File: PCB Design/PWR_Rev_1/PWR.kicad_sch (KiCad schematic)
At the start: 57 parts, among them J1 Conn_01x24_Pin, J2 Conn_01x24_Pin, U1 LMR33630ADDA, U2 LMR33630ADDA, U3 LMR33630ADDA

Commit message: Cleaned up Formating
Cleaned up formatting and added required exports for delivery
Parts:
- R7: value 100k -> N/A
- R9: value 9.09k -> N/A
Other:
- note added: "BOARD CONNECTORS"
- company: (none) -> CAPSTONE
- title: (none) -> SWARM PWR BOARD
- moved on the sheet: C28, C29, D1, D2, D3, D4, D5, F1, H1, H2, J1, J2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

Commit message: Small Updates
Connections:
- net GND: now also D5.2 (A); no longer D5.1 (K)
- net at D4.2 (A), F1.2: now also D5.1 (K); no longer D5.2 (A)
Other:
- moved on the sheet: D5
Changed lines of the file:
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@@
 	(symbol
 		(lib_id "Diode:PTVS5V0Z1USK")
-		(at 148.59 105.41 90)
+		(at 148.59 105.41 270)
 		(unit 1)
 		(exclude_from_sim no)
@@
 		(dnp no)
 		(property "Reference" "D5"
-			(at 149.86 105.41 90)
+			(at 147.32 105.41 90)
 			(effects
 				(font
@@
 		)
 		(property "Value" "SMBJ18A"
-			(at 148.844 107.95 90)
+			(at 148.082 107.95 90)
 			(effects
 				(font
@@
 		)
 		(property "Footprint" "Diode_SMD:D_SMB"
-			(at 153.035 105.41 0)
+			(at 144.145 105.41 0)
 			(effects
 				(font

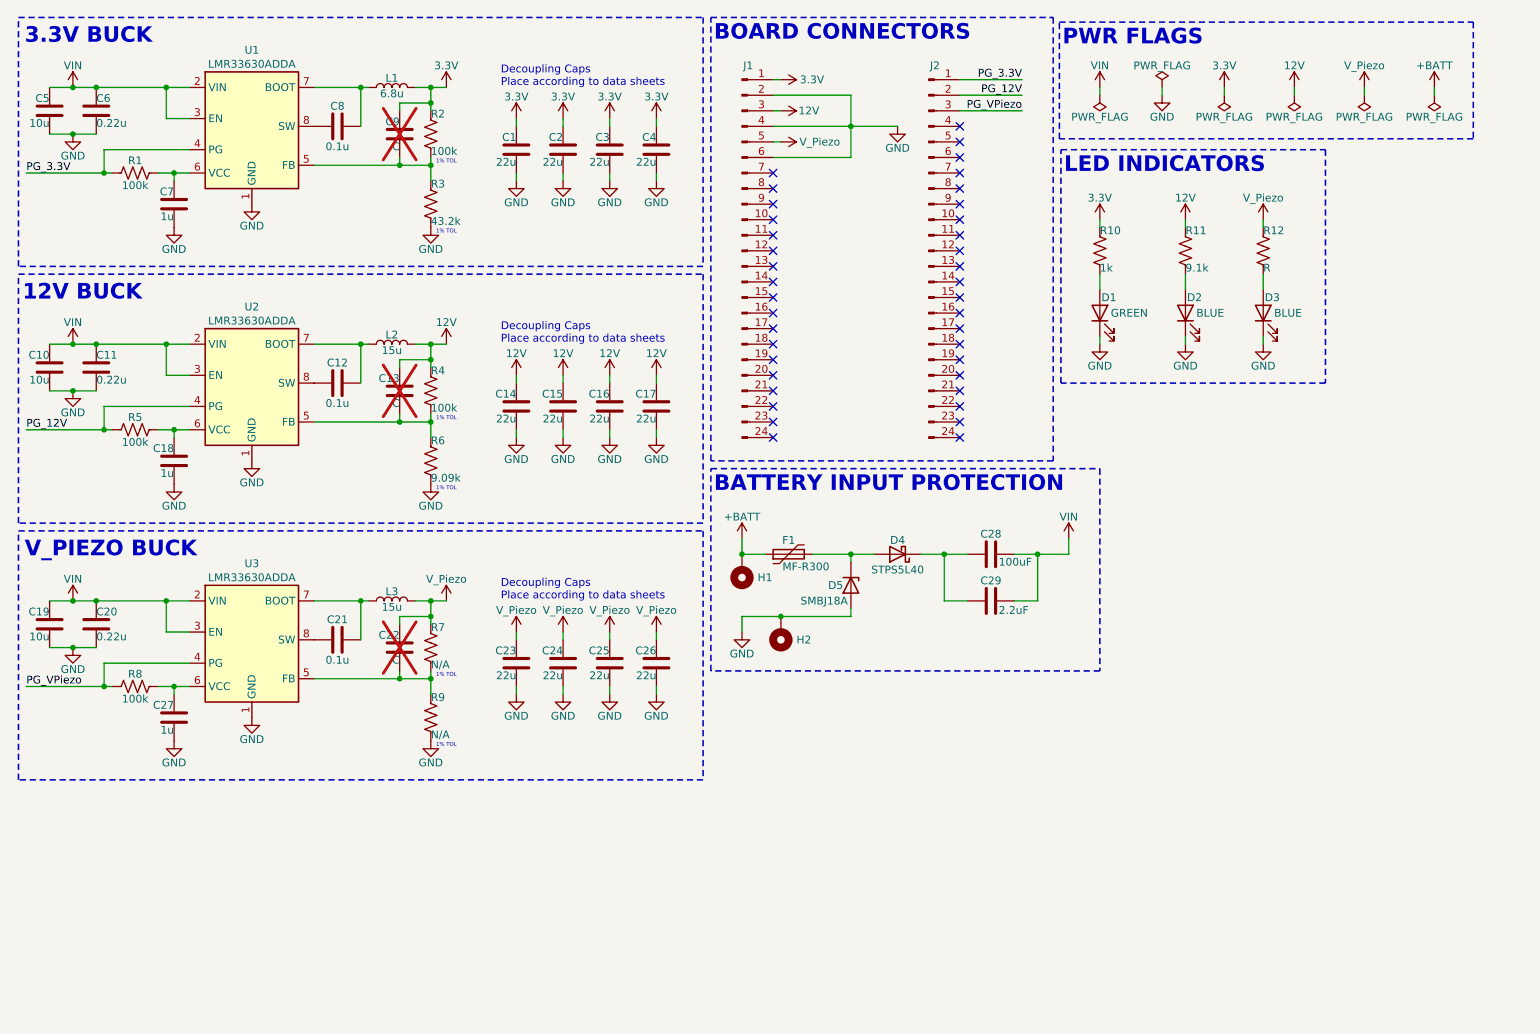
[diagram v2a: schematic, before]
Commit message: Fixed Schematic Errors
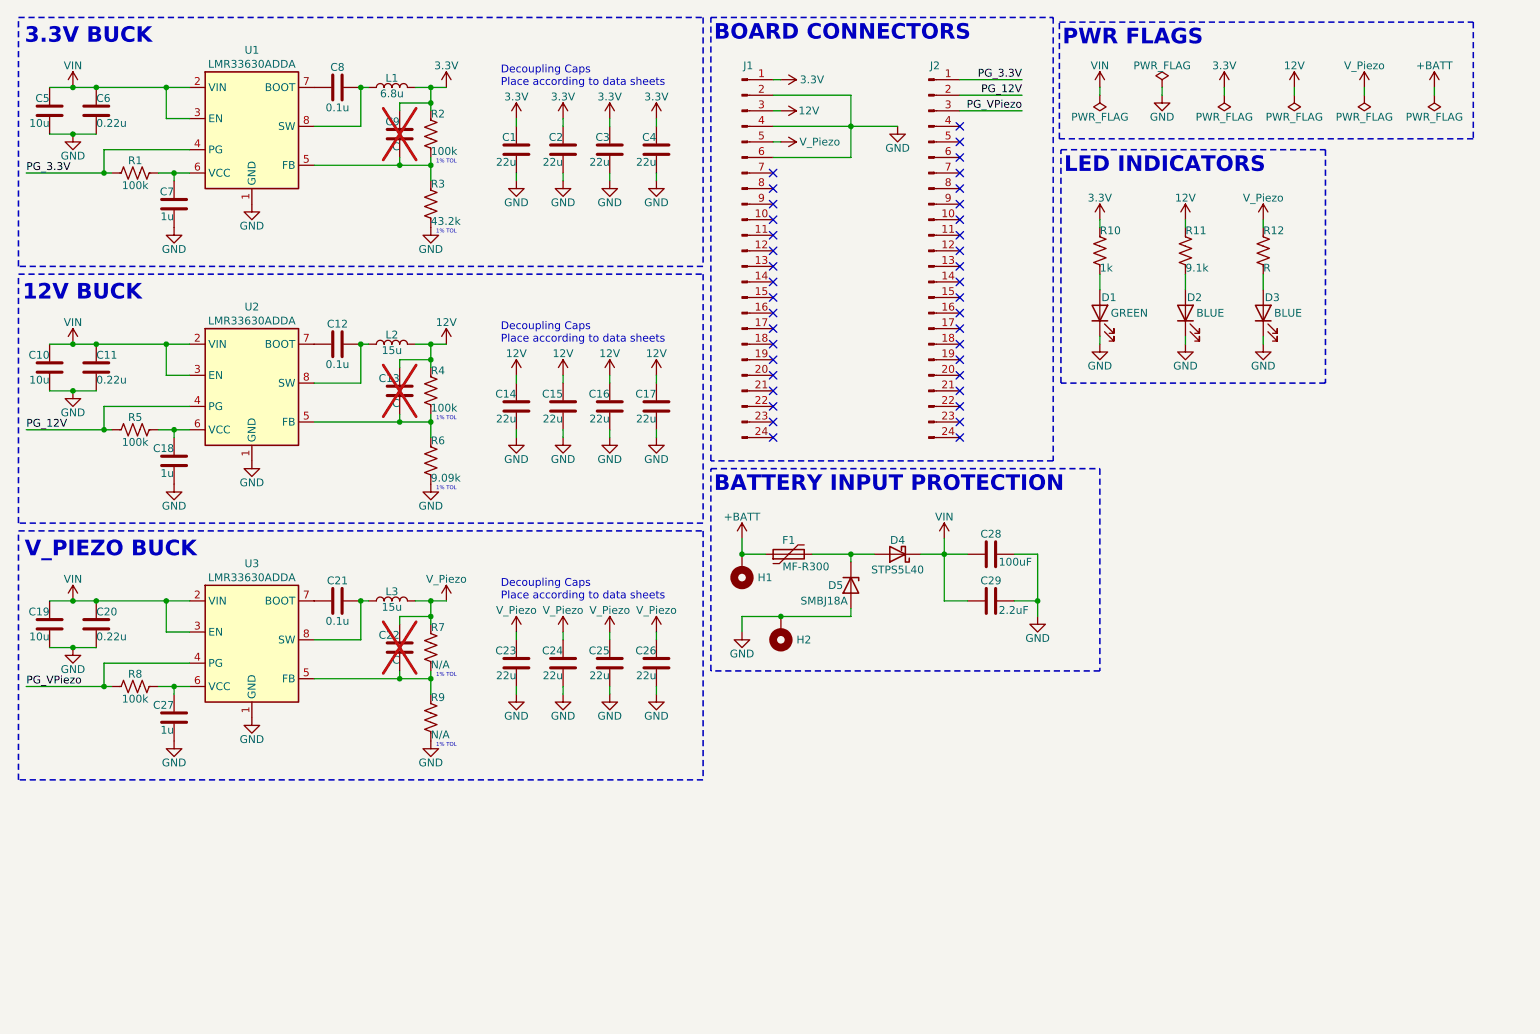
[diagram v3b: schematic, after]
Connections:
- net GND: now also C28.2, C29.2
- net VIN: now also C28.1, C29.1, D4.1 (K); no longer C28.2, C29.2
- net at C12.1, L2.1: now also U2.8 (SW); no longer U2.7 (BOOT)
- net at C12.2: now also U2.7 (BOOT); no longer U2.8 (SW)
- net at C8.1, L1.1: now also U1.8 (SW); no longer U1.7 (BOOT)
- net at C8.2: now also U1.7 (BOOT); no longer U1.8 (SW)
- net at C21.1, L3.1: now also U3.8 (SW); no longer U3.7 (BOOT)
- net at C21.2: now also U3.7 (BOOT); no longer U3.8 (SW)
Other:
- moved on the sheet: C12, C21, C8

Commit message: Added PWR Export Files
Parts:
- L3: value 15u -> N/A
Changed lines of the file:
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@@
 	(title_block
 		(title "SWARM PWR BOARD")
-		(date "2026-03-21")
+		(date "2026-03-23")
 		(rev "1.1")
 		(company "CAPSTONE")
@@
 			)
 		)
-		(property "Value" "15u"
+		(property "Value" "N/A"
 			(at 73.66 108.966 90)
 			(effects

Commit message: PWR - Updated 3D Models for Full Board Export
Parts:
- F1: footprint Fuse:Fuse_Bourns_MF-RHT300 -> PWR_Library:Fuse_Bourns_MF-RHT300
- L1, L2, L3: footprint Inductor_SMD:L_Wuerth_MAPI-5030 -> PWR_Library:L_Wuerth_MAPI-5030
- U1, U2, U3: footprint Package_SO:Texas_HSOP-8-1EP_3.9x4.9mm_P1.27mm_ThermalVias -> PWR_Library:Texas_HSOP-8-1EP_3.9x4.9mm_P1.27mm_ThermalVias
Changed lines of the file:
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@@
 			)
 		)
-		(property "Footprint" "Package_SO:Texas_HSOP-8-1EP_3.9x4.9mm_P1.27mm_ThermalVias"
+		(property "Footprint" "PWR_Library:Texas_HSOP-8-1EP_3.9x4.9mm_P1.27mm_ThermalVias"
 			(at 50.8 91.44 0)
 			(effects
@@
 			)
 		)
-		(property "Footprint" "Inductor_SMD:L_Wuerth_MAPI-5030"
+		(property "Footprint" "PWR_Library:L_Wuerth_MAPI-5030"
 			(at 73.66 66.04 0)
 			(effects
@@
 			)
 		)
-		(property "Footprint" "Fuse:Fuse_Bourns_MF-RHT300"
+		(property "Footprint" "PWR_Library:Fuse_Bourns_MF-RHT300"
 			(at 143.51 99.06 0)
 			(effects
@@
 			)
 		)
-		(property "Footprint" "Package_SO:Texas_HSOP-8-1EP_3.9x4.9mm_P1.27mm_ThermalVias"
+		(property "Footprint" "PWR_Library:Texas_HSOP-8-1EP_3.9x4.9mm_P1.27mm_ThermalVias"
 			(at 50.8 49.53 0)
 			(effects
@@
 			)
 		)
-		(property "Footprint" "Inductor_SMD:L_Wuerth_MAPI-5030"
+		(property "Footprint" "PWR_Library:L_Wuerth_MAPI-5030"
 			(at 73.66 24.13 0)
 			(effects
@@
 			)
 		)
-		(property "Footprint" "Inductor_SMD:L_Wuerth_MAPI-5030"
+		(property "Footprint" "PWR_Library:L_Wuerth_MAPI-5030"
 			(at 73.66 107.95 0)
 			(effects
@@
 			)
 		)
-		(property "Footprint" "Package_SO:Texas_HSOP-8-1EP_3.9x4.9mm_P1.27mm_ThermalVias"
+		(property "Footprint" "PWR_Library:Texas_HSOP-8-1EP_3.9x4.9mm_P1.27mm_ThermalVias"
 			(at 50.8 133.35 0)
 			(effects

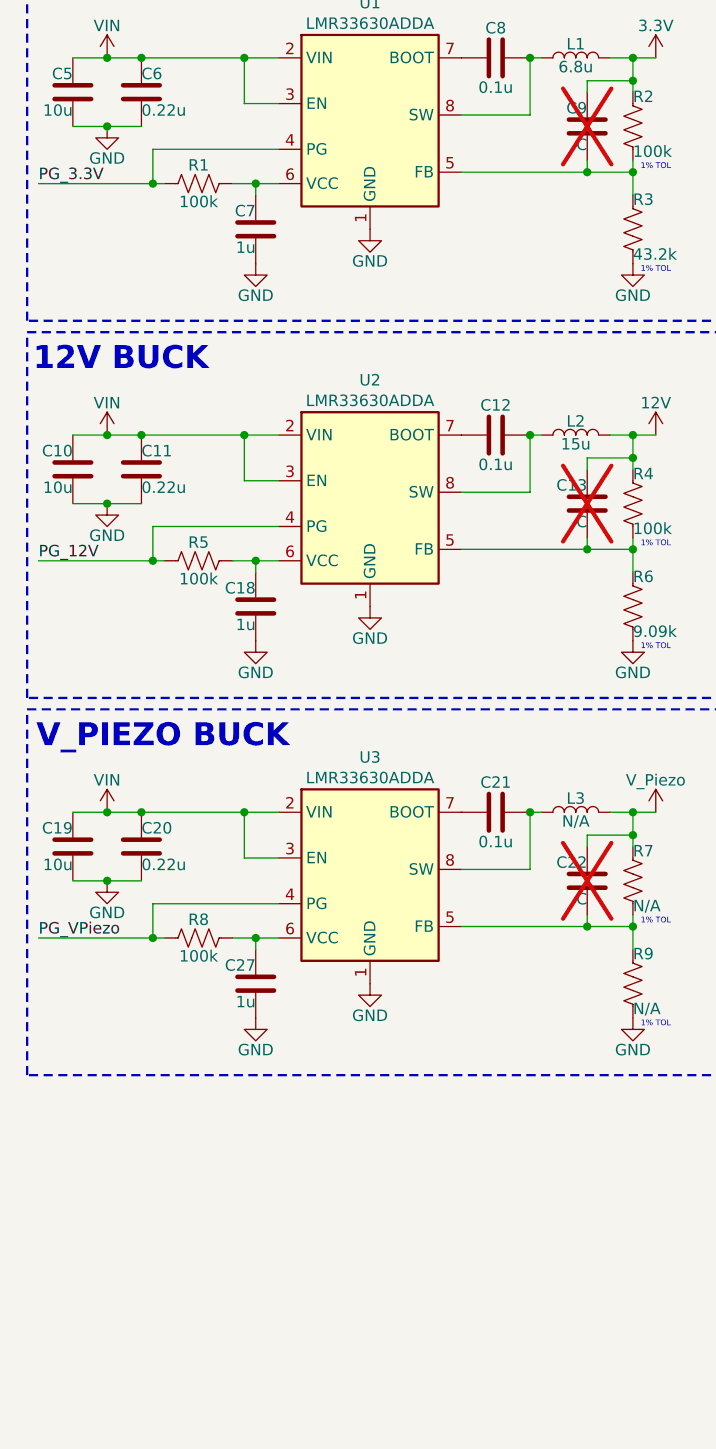
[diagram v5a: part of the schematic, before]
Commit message: Added Voltage Divider
Added Voltage Divider to 3.3PG and 12VPG
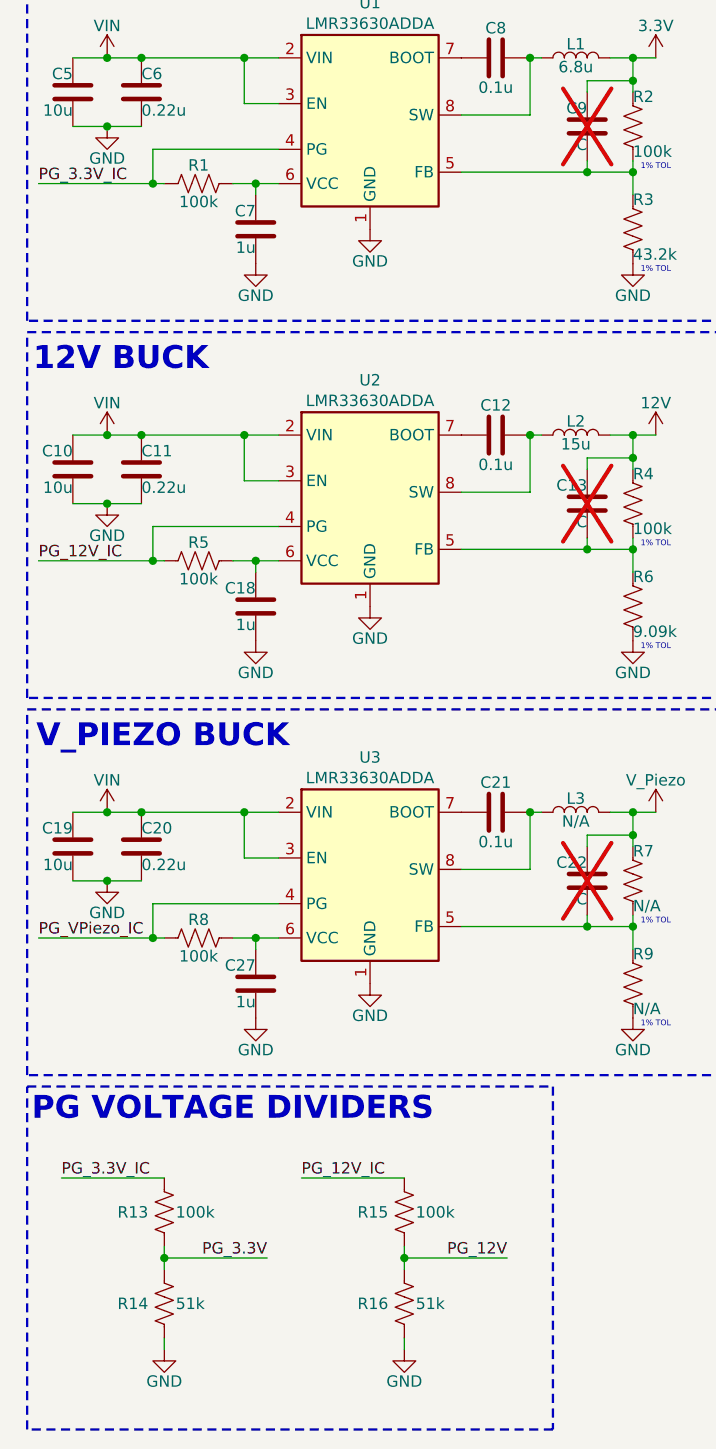
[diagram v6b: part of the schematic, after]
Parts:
- added R13, R15: 100k, Resistor_SMD:R_0603_1608Metric, symbol Device:R_US
- added R14, R16: 51k, Resistor_SMD:R_0603_1608Metric, symbol Device:R_US
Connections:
- net GND: now also R14.1, R16.1
- net PG_12V: now also R15.1, R16.2; no longer R5.1, U2.4 (PG)
- net PG_3.3V: now also R13.1, R14.2; no longer R1.1, U1.4 (PG)
- net PG_VPiezo: no longer R8.1, U3.4 (PG)
- new net PG_12V_IC: R15.2, R5.1, U2.4 (PG)
- new net PG_3.3V_IC: R1.1, R13.2, U1.4 (PG)
- new net PG_VPiezo_IC: R8.1, U3.4 (PG)
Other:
- note added: "PG VOLTAGE DIVIDERS"
